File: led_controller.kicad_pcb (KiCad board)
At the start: 2 copper layers, 88.9 x 46.2 mm, 83 parts, among them J1 Screw_Terminal_01x02, J10 Conn_01x03, J2 SJ-3524-SMT, J3 Conn_01x03, J4 Conn_01x03, J5 Conn_01x03, J6 Conn_01x03, J7 Conn_01x03, J8 Conn_01x03, J9 Conn_01x03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

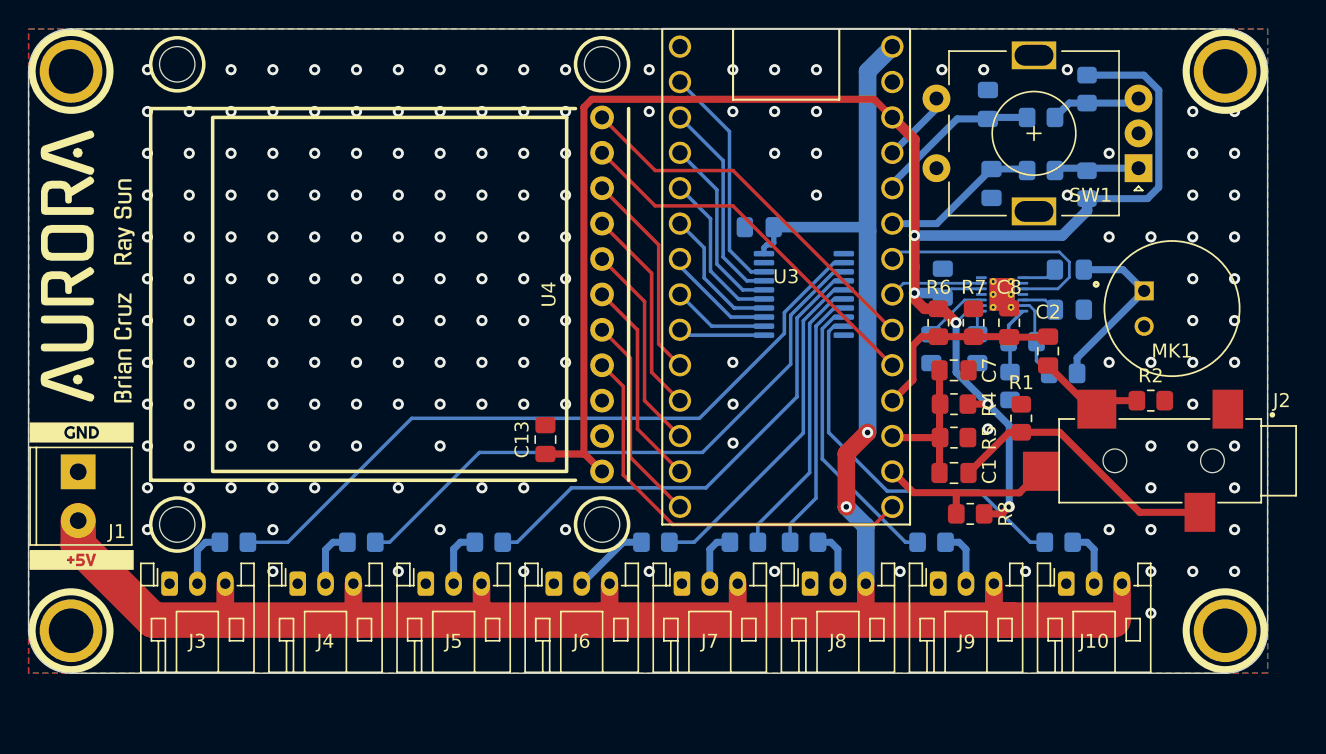
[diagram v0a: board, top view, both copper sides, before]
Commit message: Switch to molex nano-fit connectors
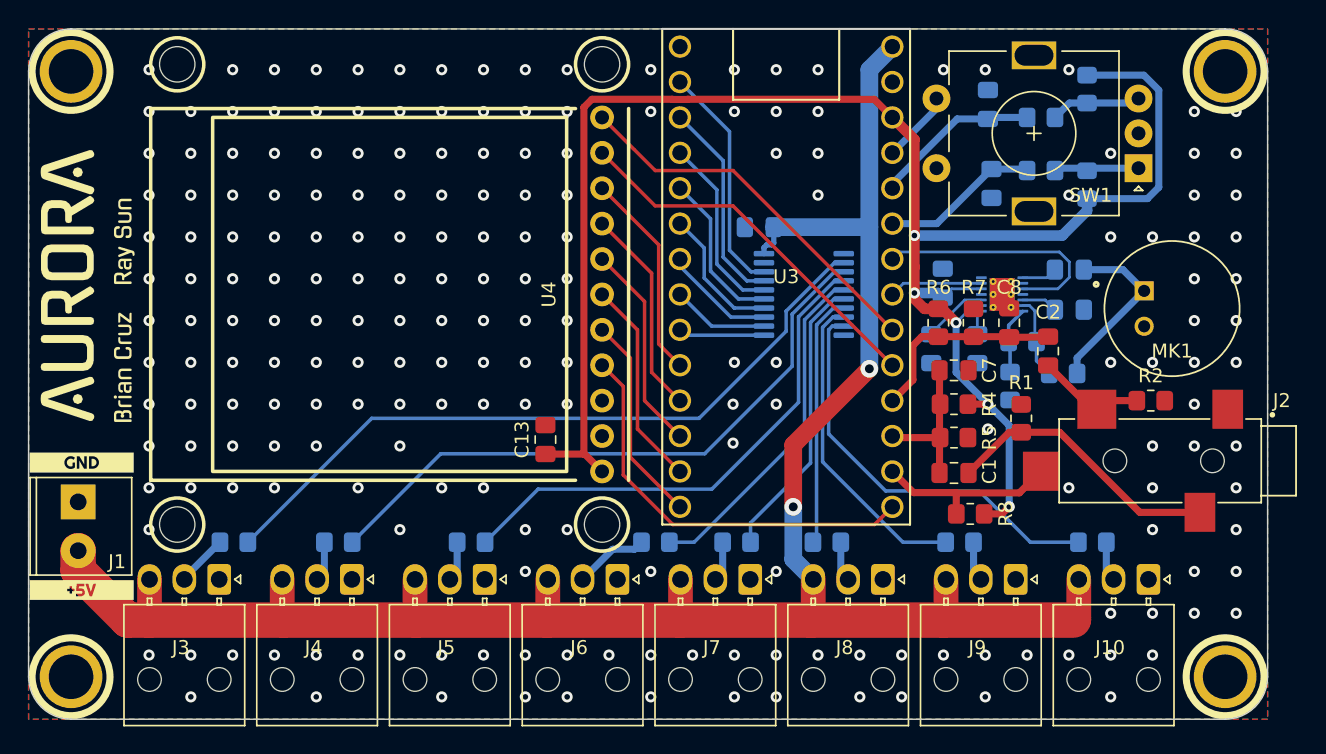
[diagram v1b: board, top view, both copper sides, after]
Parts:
- removed kibuzzard-62AD6AEC, kibuzzard-62AD6AEC1, kibuzzard-62AD6AEC2, kibuzzard-62AD6AEC3, kibuzzard-62AD6AEC4, kibuzzard-62AD6AEC5, kibuzzard-62AD6AEC6, kibuzzard-62AD6AEC7: G***, kibuzzard-62AD6AEC
- removed kibuzzard-62AD6B04, kibuzzard-62AD6B1, kibuzzard-62AD6B2, kibuzzard-62AD6B3, kibuzzard-62AD6B4, kibuzzard-62AD6B5, kibuzzard-62AD6B6, kibuzzard-62AD6B7: G***, kibuzzard-62AD6B04
- removed kibuzzard-62AD6B13: G***, kibuzzard-62AD6B13
- removed kibuzzard-62AD6BA8: G***, kibuzzard-62AD6BA8
- removed kibuzzard-62AD6BC2: G***, kibuzzard-62AD6BC2
- removed kibuzzard-62AD6C16: G***, kibuzzard-62AD6C16
- removed kibuzzard-62AD6C27: G***, kibuzzard-62AD6C27
- removed kibuzzard-62AD6C38: G***, kibuzzard-62AD6C38
- removed kibuzzard-62AD6C4C: G***, kibuzzard-62AD6C4C
- removed kibuzzard-62AD6C62: G***, kibuzzard-62AD6C62
- J10, J3, J4, J5, J6, J7, J8, J9: footprint Connector_JST:JST_PH_S3B-PH-K_1x03_P2.00mm_Horizontal -> Connector_Molex:Molex_Nano-Fit_105313-xx03_1x03_P2.50mm_Horizontal
- moved J10 5.90 mm to (170.5, 126.6), turned to -90 degrees
- moved J9 5.57 mm to (161.0, 126.6), turned to -90 degrees
- moved J8 5.24 mm to (151.5, 126.6), turned to -90 degrees
- moved J7 4.91 mm to (141.9, 126.6), turned to -90 degrees
- moved J6 4.57 mm to (132.4, 126.6), turned to -90 degrees
- moved J5 4.24 mm to (122.9, 126.6), turned to -90 degrees
- moved J4 3.91 mm to (113.4, 126.6), turned to -90 degrees
- moved J3 3.57 mm to (103.8, 126.6), turned to -90 degrees
- moved H3 3.30 mm to (93.2, 133.6)
- moved H4 3.30 mm to (176.0, 133.6)
- moved R20 2.41 mm to (166.5, 124.0)
- moved kibuzzard-62AD66A7 2.16 mm to (94.0, 127.4)
- moved J1 2.16 mm to (93.7, 121.1)
- moved kibuzzard-62AD66B6 2.16 mm to (94.0, 118.2)
- moved R19 2.02 mm to (157.0, 124.0)
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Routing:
- net Net-(R20-Pad2): track 27.3 -> 29.8 mm
- net Net-(R19-Pad2): track 20.5 -> 22.7 mm
- net Net-(R14-Pad2): track 43.7 -> 45.5 mm
- net +5V: track 150.9 -> 149.2 mm
- net Net-(R15-Pad2): track 35.6 -> 37.1 mm
- net /LED_OUT_1: track 4.23 -> 2.88 mm
- net /LED_OUT_7: track 4.22 -> 2.88 mm
- net /LED_OUT_2: track 4.21 -> 2.88 mm
- net /LED_OUT_6: track 4.15 -> 2.88 mm
- net /LED_OUT_4: track 4.12 -> 2.88 mm
- net /LED_OUT_5: track 4.11 -> 2.88 mm
- net Net-(R18-Pad2): track 18.8 -> 18.2 mm
- net /LED_OUT_0: track 4.25 -> 3.73 mm
- net GND: vias 175 -> 210
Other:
- board size 88.9 x 46.2 mm -> 88.9 x 49.5 mm

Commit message: Revert "Switch to molex nano-fit connectors"
This reverts commit 9b38a182e228fa806dde65dc415f981188c8a403.
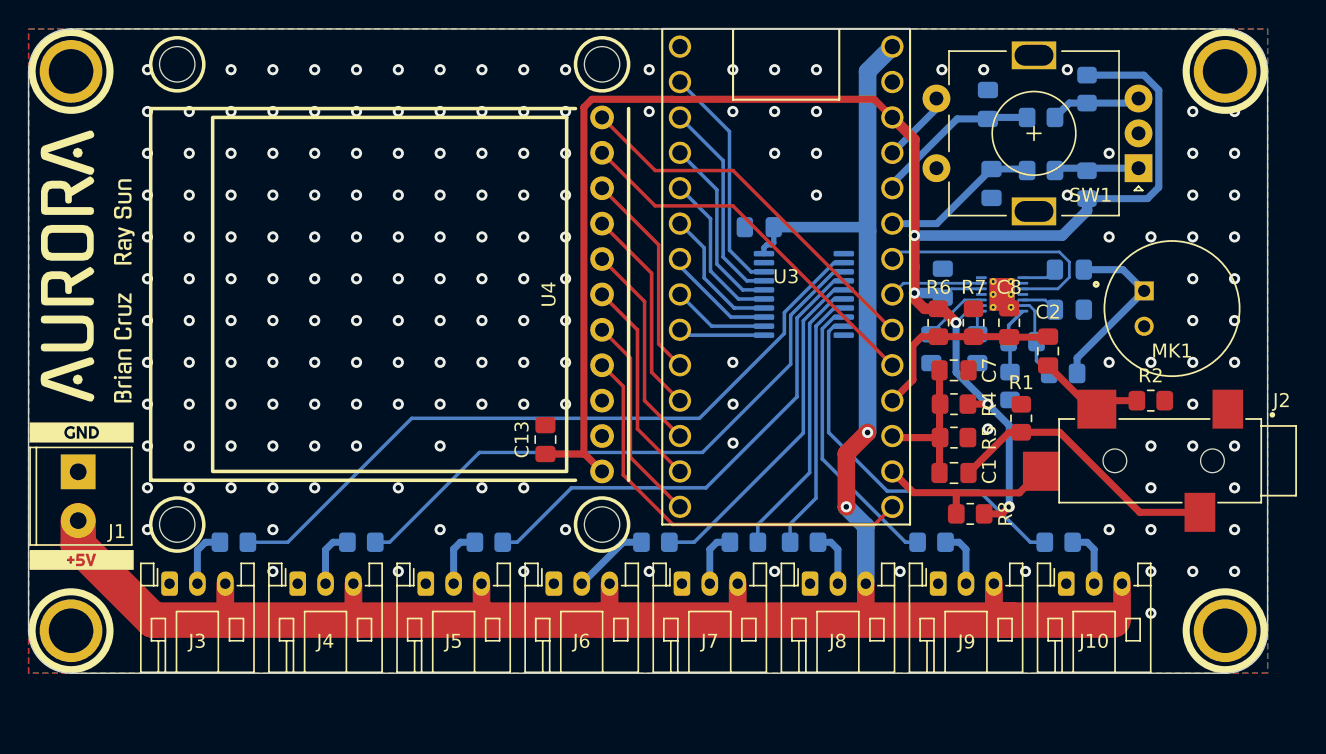
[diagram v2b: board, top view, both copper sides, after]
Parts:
- added kibuzzard-62AD6AEC: G***, kibuzzard-62AD6AEC, B.Cu at (100.3, 131.3)
- added kibuzzard-62AD6AEC1: G***, kibuzzard-62AD6AEC, B.Cu at (109.5, 131.3)
- added kibuzzard-62AD6AEC2: G***, kibuzzard-62AD6AEC, B.Cu at (118.7, 131.3)
- added kibuzzard-62AD6AEC3: G***, kibuzzard-62AD6AEC, B.Cu at (127.9, 131.3)
- added kibuzzard-62AD6AEC4: G***, kibuzzard-62AD6AEC, B.Cu at (137.1, 131.3)
- added kibuzzard-62AD6AEC5: G***, kibuzzard-62AD6AEC, B.Cu at (146.2, 131.3)
- added kibuzzard-62AD6AEC6: G***, kibuzzard-62AD6AEC, B.Cu at (155.4, 131.3)
- added kibuzzard-62AD6AEC7: G***, kibuzzard-62AD6AEC, B.Cu at (164.6, 131.3)
- added kibuzzard-62AD6B04: G***, kibuzzard-62AD6B04, B.Cu at (104.3, 131.3)
- added kibuzzard-62AD6B1: G***, kibuzzard-62AD6B04, B.Cu at (113.5, 131.3)
- added kibuzzard-62AD6B13: G***, kibuzzard-62AD6B13, B.Cu at (102.3, 131.3)
- added kibuzzard-62AD6B2: G***, kibuzzard-62AD6B04, B.Cu at (122.7, 131.3)
- added kibuzzard-62AD6B3: G***, kibuzzard-62AD6B04, B.Cu at (131.9, 131.3)
- added kibuzzard-62AD6B4: G***, kibuzzard-62AD6B04, B.Cu at (141.1, 131.3)
- added kibuzzard-62AD6B5: G***, kibuzzard-62AD6B04, B.Cu at (150.2, 131.3)
- added kibuzzard-62AD6B6: G***, kibuzzard-62AD6B04, B.Cu at (159.4, 131.3)
- added kibuzzard-62AD6B7: G***, kibuzzard-62AD6B04, B.Cu at (168.6, 131.3)
- added kibuzzard-62AD6BA8: G***, kibuzzard-62AD6BA8, B.Cu at (111.5, 131.3)
- added kibuzzard-62AD6BC2: G***, kibuzzard-62AD6BC2, B.Cu at (120.7, 131.3)
- added kibuzzard-62AD6C16: G***, kibuzzard-62AD6C16, B.Cu at (129.9, 131.3)
- added kibuzzard-62AD6C27: G***, kibuzzard-62AD6C27, B.Cu at (139.0, 131.3)
- added kibuzzard-62AD6C38: G***, kibuzzard-62AD6C38, B.Cu at (148.2, 131.3)
- added kibuzzard-62AD6C4C: G***, kibuzzard-62AD6C4C, B.Cu at (157.4, 131.3)
- added kibuzzard-62AD6C62: G***, kibuzzard-62AD6C62, B.Cu at (166.6, 131.3)
- J10, J3, J4, J5, J6, J7, J8, J9: footprint Connector_Molex:Molex_Nano-Fit_105313-xx03_1x03_P2.50mm_Horizontal -> Connector_JST:JST_PH_S3B-PH-K_1x03_P2.00mm_Horizontal
- moved J10 5.90 mm to (164.6, 126.9), turned to 0 degrees
- moved J9 5.57 mm to (155.4, 126.9), turned to 0 degrees
- moved J8 5.24 mm to (146.2, 126.9), turned to 0 degrees
- moved J7 4.91 mm to (137.1, 126.9), turned to 0 degrees
- moved J6 4.57 mm to (127.9, 126.9), turned to 0 degrees
- moved J5 4.24 mm to (118.7, 126.9), turned to 0 degrees
- moved J4 3.91 mm to (109.5, 126.9), turned to 0 degrees
- moved J3 3.57 mm to (100.3, 126.9), turned to 0 degrees
- moved H3 3.30 mm to (93.2, 130.3)
- moved H4 3.30 mm to (176.0, 130.3)
- moved R20 2.41 mm to (164.1, 124.0)
- moved kibuzzard-62AD66A7 2.16 mm to (94.0, 125.2)
- moved J1 2.16 mm to (93.7, 118.9)
- moved kibuzzard-62AD66B6 2.16 mm to (94.0, 116.1)
- moved R19 2.02 mm to (155.0, 124.0)
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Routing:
- net Net-(R20-Pad2): track 29.8 -> 27.3 mm
- net Net-(R19-Pad2): track 22.7 -> 20.5 mm
- net Net-(R14-Pad2): track 45.5 -> 43.7 mm
- net +5V: track 149.2 -> 150.9 mm
- net Net-(R15-Pad2): track 37.1 -> 35.6 mm
- net /LED_OUT_1: track 2.88 -> 4.23 mm
- net /LED_OUT_7: track 2.88 -> 4.22 mm
- net /LED_OUT_2: track 2.88 -> 4.21 mm
- net /LED_OUT_6: track 2.88 -> 4.15 mm
- net /LED_OUT_4: track 2.88 -> 4.12 mm
- net /LED_OUT_5: track 2.88 -> 4.11 mm
- net Net-(R18-Pad2): track 18.2 -> 18.8 mm
- net /LED_OUT_0: track 3.73 -> 4.25 mm
- net GND: vias 210 -> 175
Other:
- board size 88.9 x 49.5 mm -> 88.9 x 46.2 mm
